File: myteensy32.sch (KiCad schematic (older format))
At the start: 14 parts, among them U1 MKL04Z32VLC4, U2 MK20DX256VLH7

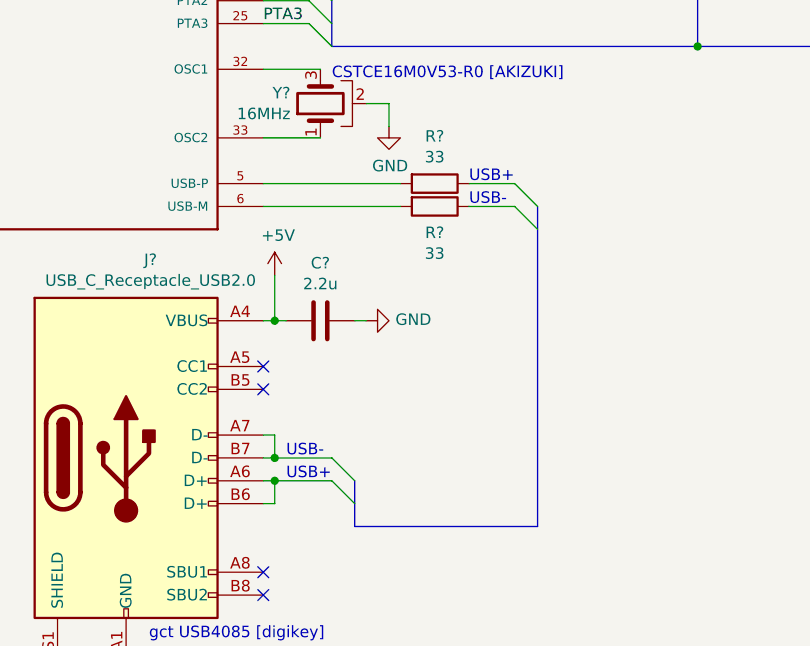
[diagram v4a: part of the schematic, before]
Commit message: ラベルのつもりがテキストになってたので修正
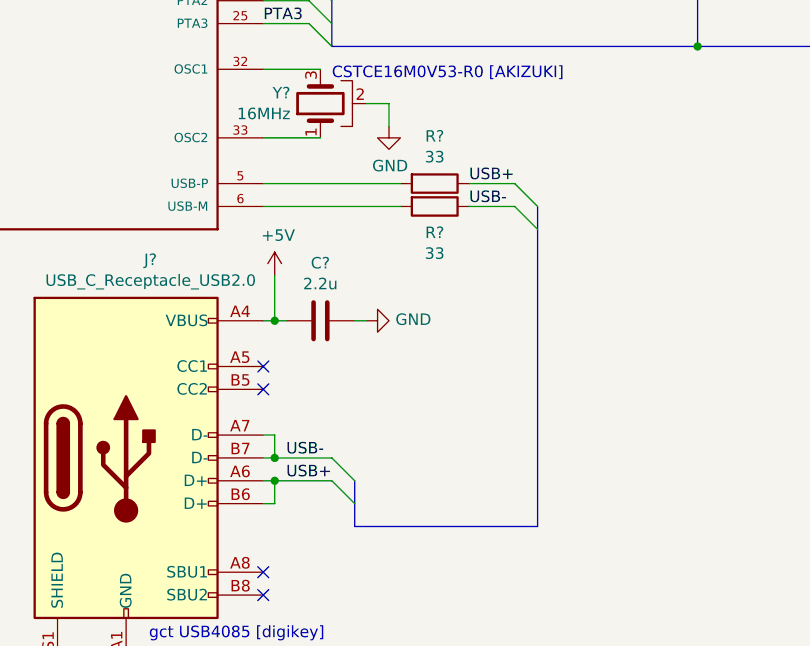
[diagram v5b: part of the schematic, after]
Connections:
- net USB+: now reaches J?.A6 (D+), J?.B6 (D+)
- net USB+: now also R?.1
- net USB-: now reaches J?.A7 (D-), J?.B7 (D-)
- net USB-: now also R?.1
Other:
- note removed: "USB+"
- note removed: "USB-"
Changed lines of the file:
@@
 Wire Wire Line
 	4850 5250 4650 5250
-Text Notes 4650 5250 0    50   ~ 0
-USB+
 Wire Wire Line
 	4650 5350 4850 5350
@@
 	1    0    0    -1
 $EndComp
-Text Notes 4650 5350 0    50   ~ 0
-USB-
 Wire Wire Line
 	3800 6450 3750 6450
@@
 	3800 6650 3750 6650
 Connection ~ 3800 6550
-Text Notes 3850 6550 0    50   ~ 0
-USB+
-Text Notes 3850 6450 0    50   ~ 0
-USB-
 $Comp
 L Device:R R?
@@
 Wire Bus Line
 	4050 4250 4050 4650
+Text Label 4650 5250 0    50   ~ 0
+USB+
+Text Label 4650 5350 0    50   ~ 0
+USB-
+Text Label 3850 6450 0    50   ~ 0
+USB-
+Text Label 3850 6550 0    50   ~ 0
+USB+
 $EndSCHEMATC

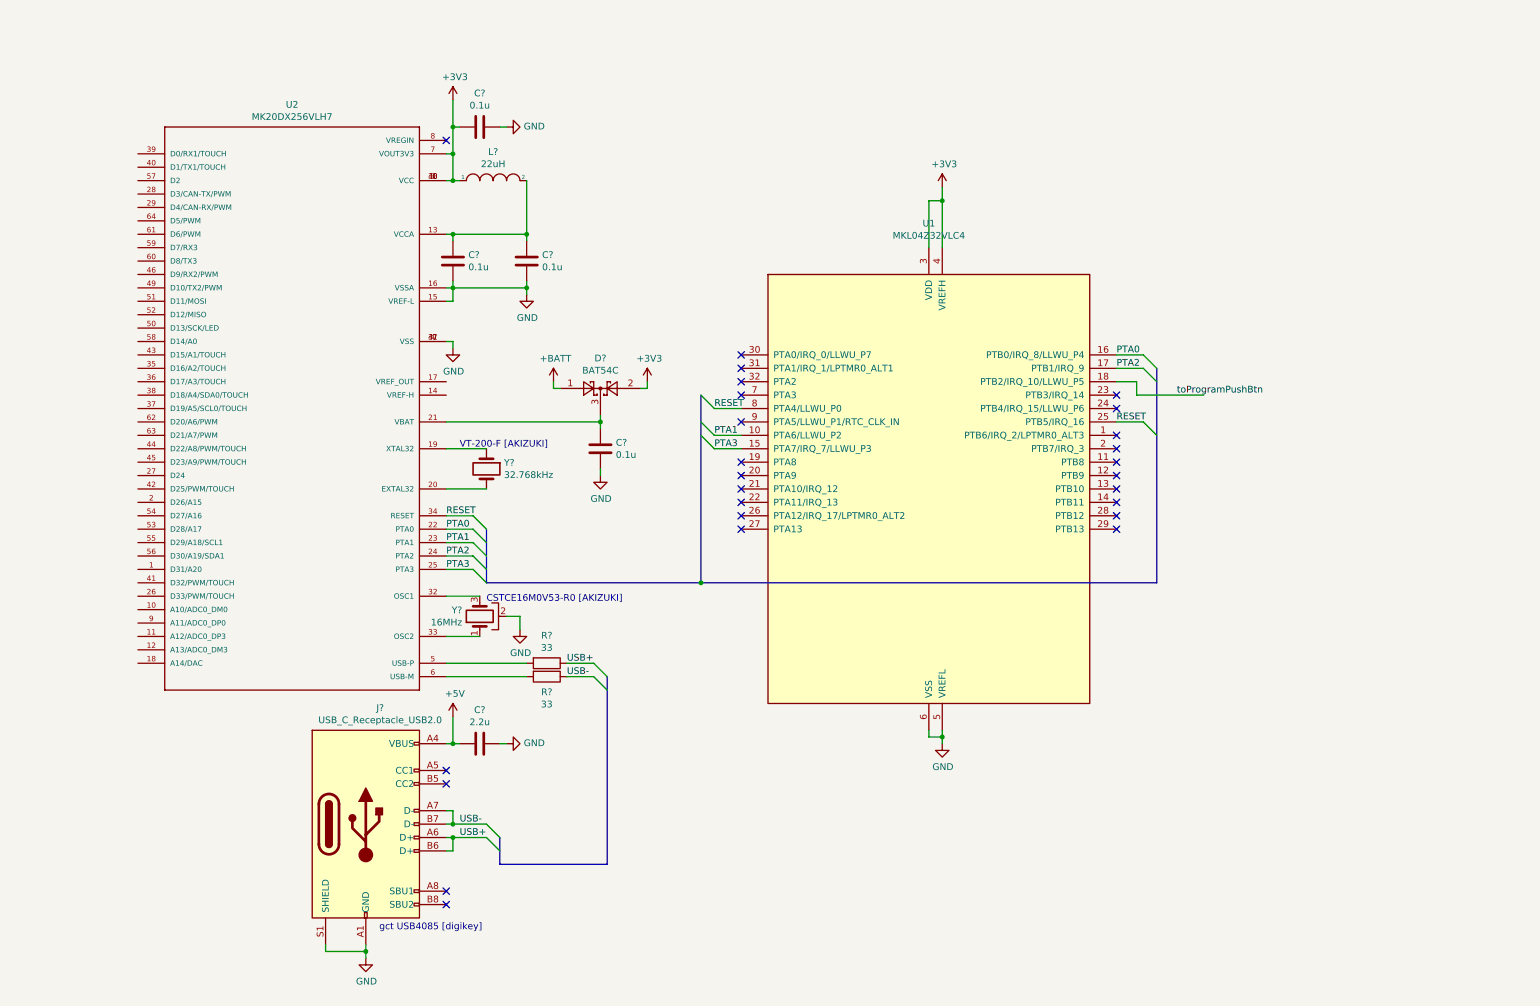
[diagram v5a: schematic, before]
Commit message: usb周辺回路、agnd等を記述
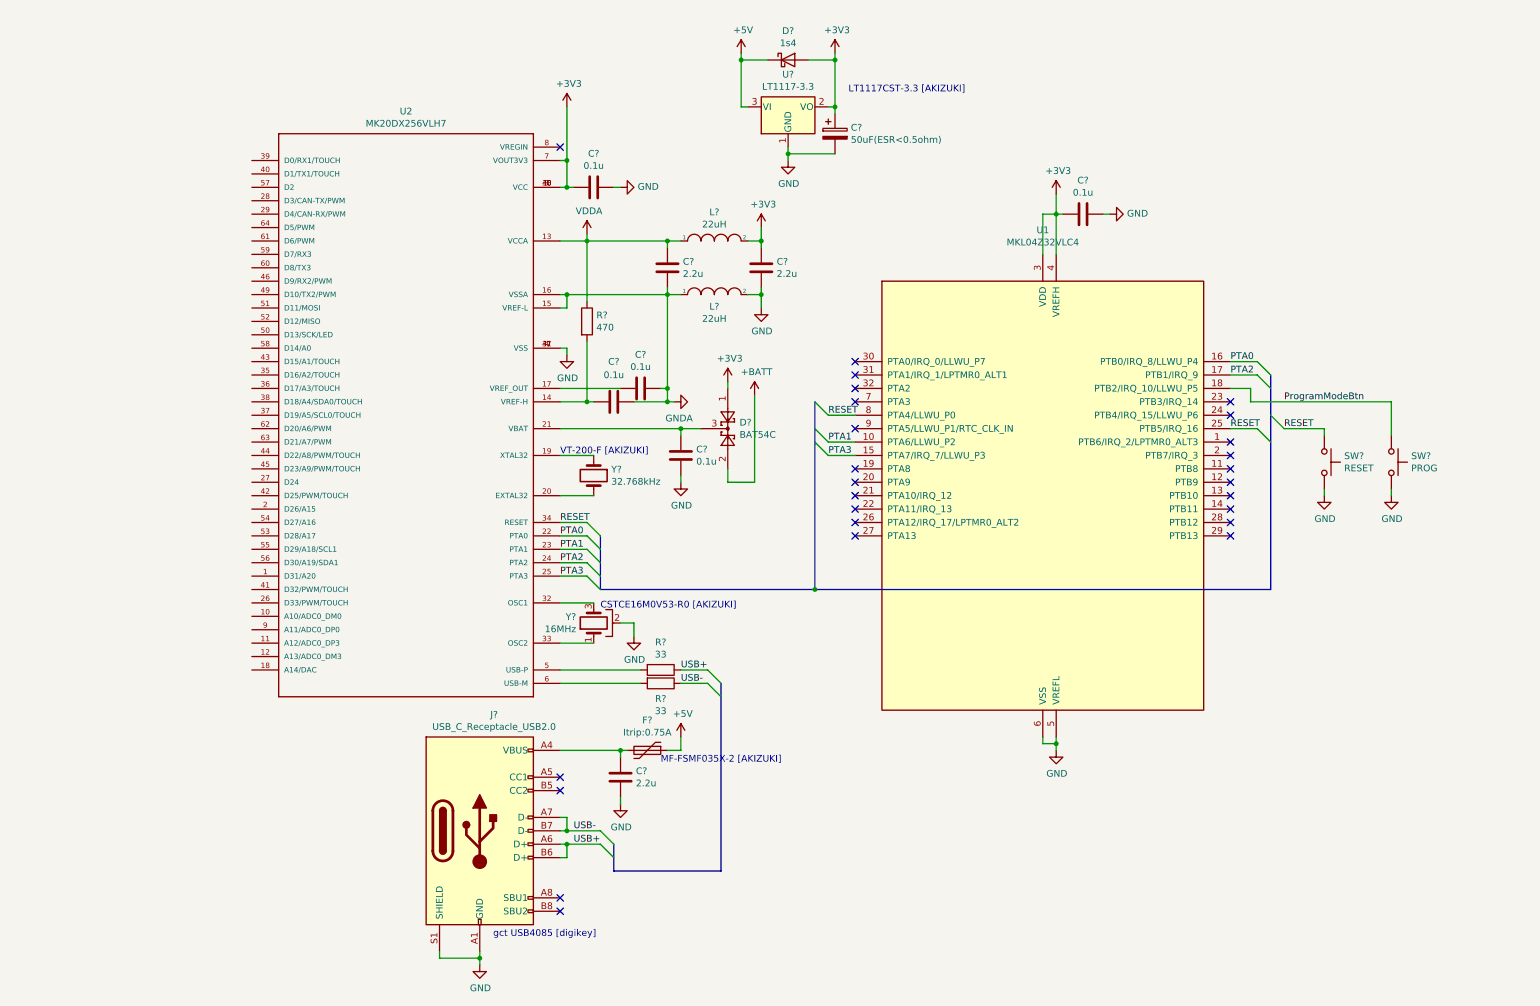
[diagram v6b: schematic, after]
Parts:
- added C? (x3): 0.1u, symbol Device:C
- added C?: 50uF(ESR<0.5ohm), symbol Device:CP
- added D?: 1s4, symbol Device:D_Schottky
- added F?: Itrip:0.75A, symbol Device:Polyfuse
- added L?: 22uH, symbol pspice:INDUCTOR
- added R?: 470, symbol Device:R
- added SW?: RESET, symbol Switch:SW_Push
- added SW?: PROG, symbol Switch:SW_Push
- added U?: LT1117-3.3, symbol Regulator_Linear:LT1117-3.3
- C? (x2): value 0.1u -> 2.2u
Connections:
- net +3V3: now also C?.1, D?.1, L?.2, C?.1, C?.2, D?.2 (A), U?.2 (VO); no longer D?.2, L?.1
- net +5V: now also D?.1 (K), F?.1, U?.3 (VI); no longer C?.2, J?.A4 (VBUS), J?.A9 (VBUS), J?.B4 (VBUS), J?.B9 (VBUS)
- net +BATT: now also D?.2; no longer D?.1
- net GND: now also C?.1, C?.2, L?.2, SW?.2, SW?.2, U?.1 (GND); no longer C?.2, U2.15 (VREF-L), U2.16 (VSSA)
- net RESET: now also SW?.1
- net VDDA: now reaches C?.1, U2.13 (VCCA)
- net VDDA: now also L?.1, R?.1; no longer C?.1, L?.2
- net at U2.14 (VREF-H): now also C?.2, R?.2
- net at U2.17 (VREF_OUT): now also C?.2
- net toProgramPushBtn renamed ProgramModeBtn
- net ProgramModeBtn: now also SW?.1
- new net: C?.2, F?.2, J?.A4 (VBUS), J?.A9 (VBUS), J?.B4 (VBUS), J?.B9 (VBUS)
- new net GNDA: C?.1, C?.1, C?.2, L?.1, U2.15 (VREF-L), U2.16 (VSSA)
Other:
- note added: "LT1117CST-3.3 [AKIZUKI]"
- note added: "MF-FSMF035X-2 [AKIZUKI]"
- moved on the sheet: C?, D?, J?, L?, R?, U1, U2, Y?

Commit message: とりあえず全部の素子にフットプリントを割り当てて大きさの余裕を見る。
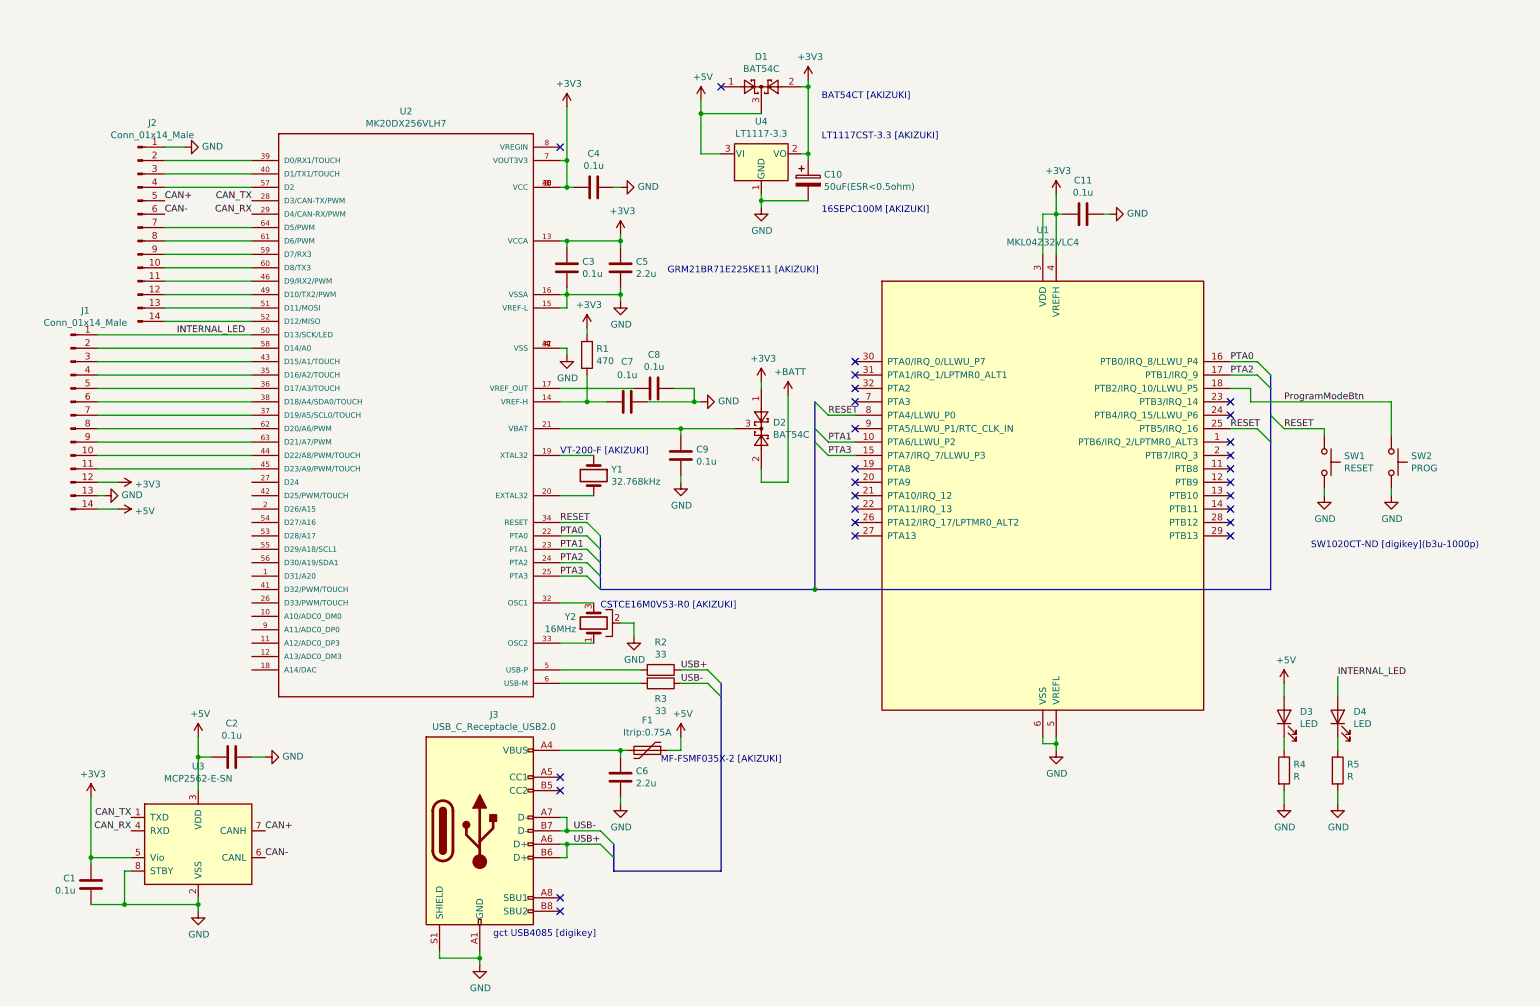
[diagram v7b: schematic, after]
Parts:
- removed C?: 2.2u, symbol Device:C
- removed D?: 1s4, symbol Device:D_Schottky
- removed L? (x2): 22uH, symbol pspice:INDUCTOR
- added C1, C2, C3: 0.1u, Capacitor_SMD:C_0603_1608Metric, symbol Device:C
- added D1: BAT54C, Package_TO_SOT_SMD:SOT-23, symbol Diode:BAT54C
- added D3, D4: LED, mylib:LED_1608_point, symbol Device:LED
- added J1, J2: Conn_01x14_Male, Connector_PinHeader_2.54mm:PinHeader_1x14_P2.54mm_Vertical, symbol Connector:Conn_01x14_Male
- added R4, R5: R, Resistor_SMD:R_0603_1608Metric, symbol Device:R
- added U3: MCP2562-E-SN, Package_SO:SOIC-8_3.9x4.9mm_P1.27mm, symbol Interface_CAN_LIN:MCP2562-E-SN
- C10: renamed from C?; footprint (none) -> Capacitor_THT:CP_Radial_D6.3mm_P2.50mm
- C11, C4, C7, C8, C9: renamed from C?; footprint (none) -> Capacitor_SMD:C_0603_1608Metric
- C5, C6: renamed from C?; footprint (none) -> Capacitor_SMD:C_0805_2012Metric
- F1: renamed from F?; footprint (none) -> Fuse:Fuse_0603_1608Metric
- J3: renamed from J?; footprint (none) -> Connector_USB:USB_C_Receptacle_GCT_USB4085
- R1, R2, R3: renamed from R?; footprint (none) -> Resistor_SMD:R_0603_1608Metric
- SW1, SW2: renamed from SW?; footprint (none) -> Button_Switch_SMD:SW_SPST_B3U-1000P
- U4: renamed from U?; footprint (none) -> Package_TO_SOT_SMD:SOT-223-3_TabPin2
- Y1: renamed from Y?; footprint (none) -> Crystal:Crystal_DS26_D2.0mm_L6.0mm_Horizontal
- Y2: renamed from Y?; footprint (none) -> mylib:CSTCE16M0V53-R0
- gave numbers to parts that had none: 1
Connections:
- net GNDA is gone; now on net GND: C5.2, C7.1, C8.1, U2.15 (VREF-L), U2.16 (VSSA)
- net VDDA is gone; now on net +3V3: C5.1, R1.1, U2.13 (VCCA)
- net +3V3: now also C1.2, C3.2, D1.2, J1.12 (Pin_12), U3.5 (Vio)
- net +5V: now also C2.2, D1.3, D3.2 (A), J1.14 (Pin_14), U3.3 (VDD)
- net GND: now also C1.1, C2.1, C3.1, J1.13 (Pin_13), J2.1 (Pin_1), R4.2, R5.2, U3.2 (VSS), U3.8 (STBY)
- net CAN_TX: now reaches U2.28 (D3/CAN-TX/PWM)
- net CAN_TX: now also U3.1 (TXD)
- net CAN_RX: now reaches U2.29 (D4/CAN-RX/PWM)
- net CAN_RX: now also U3.4 (RXD)
- net at U2.35 (D16/A2/TOUCH): now also J1.4 (Pin_4)
- net at U2.36 (D17/A3/TOUCH): now also J1.5 (Pin_5)
- net at U2.37 (D19/A5/SCL0/TOUCH): now also J1.7 (Pin_7)
- net at U2.38 (D18/A4/SDA0/TOUCH): now also J1.6 (Pin_6)
- net at U2.39 (D0/RX1/TOUCH): now also J2.2 (Pin_2)
- net at U2.40 (D1/TX1/TOUCH): now also J2.3 (Pin_3)
- net at U2.43 (D15/A1/TOUCH): now also J1.3 (Pin_3)
- net at U2.44 (D22/A8/PWM/TOUCH): now also J1.10 (Pin_10)
- net at U2.45 (D23/A9/PWM/TOUCH): now also J1.11 (Pin_11)
- net at U2.46 (D9/RX2/PWM): now also J2.11 (Pin_11)
- net at U2.49 (D10/TX2/PWM): now also J2.12 (Pin_12)
- net INTERNAL_LED: now reaches U2.50 (D13/SCK/LED)
- net INTERNAL_LED: now also D4.2 (A), J1.1 (Pin_1)
- net at U2.51 (D11/MOSI): now also J2.13 (Pin_13)
- net at U2.52 (D12/MISO): now also J2.14 (Pin_14)
- net at U2.57 (D2): now also J2.4 (Pin_4)
- net at U2.58 (D14/A0): now also J1.2 (Pin_2)
- net at U2.59 (D7/RX3): now also J2.9 (Pin_9)
- net at U2.60 (D8/TX3): now also J2.10 (Pin_10)
- net at U2.61 (D6/PWM): now also J2.8 (Pin_8)
- net at U2.62 (D20/A6/PWM): now also J1.8 (Pin_8)
- net at U2.63 (D21/A7/PWM): now also J1.9 (Pin_9)
- net at U2.64 (D5/PWM): now also J2.7 (Pin_7)
- new net: D3.1 (K), R4.1
- new net: D4.1 (K), R5.1
- new net CAN+: J2.5 (Pin_5), U3.7 (CANH)
- new net CAN-: J2.6 (Pin_6), U3.6 (CANL)
- no-connect marks 26 -> 27
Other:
- note added: "16SEPC100M [AKIZUKI]"
- note added: "BAT54CT [AKIZUKI]"
- note added: "GRM21BR71E225KE11 [AKIZUKI]"
- note added: "SW1020CT-ND [digikey](b3u-1000p)"
- moved on the sheet: C10, C5, C7, C8, D2, R1, U4

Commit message: rtc用の水晶は面積の問題と使わないので削除
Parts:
- removed Y1: 32.768kHz, Crystal:Crystal_DS26_D2.0mm_L6.0mm_Horizontal, symbol Device:Crystal
- C10: footprint Capacitor_THT:CP_Radial_D6.3mm_P2.50mm -> Capacitor_SMD:C_1206_3216Metric
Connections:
- net +BATT: no longer names the net of D2.2
- no-connect marks 27 -> 30
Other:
- note added: "JMK316ABJ107ML-T [AKIZUKI](100uF,6.3v)"
- note removed: "16SEPC100M [AKIZUKI]"
- note removed: "VT-200-F [AKIZUKI]"
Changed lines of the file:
@@
 	1    0    0    -1
 $EndComp
-$Comp
-L Device:Crystal Y1
-U 1 1 5F4C8EEC
-P 4850 3850
-F 0 "Y1" V 4804 3981 50  0000 L CNN
-F 1 "32.768kHz" V 4895 3981 50  0000 L CNN
-F 2 "Crystal:Crystal_DS26_D2.0mm_L6.0mm_Horizontal" H 4850 3850 50  0001 C CNN
-F 3 "~" H 4850 3850 50  0001 C CNN
-	1    4850 3850
-	0    1    1    0
-$EndComp
-Wire Wire Line
-	4850 3700 4600 3700
-Wire Wire Line
-	4850 4000 4600 4000
 Wire Wire Line
 	4850 4800 4600 4800
@@
 Wire Wire Line
 	5150 4950 5050 4950
-Text Notes 4600 3700 0    50   ~ 0
-VT-200-F [AKIZUKI]
 $Comp
 L Diode:BAT54C D2
@@
 Wire Wire Line
 	6100 3150 6100 3200
-$Comp
-L power:+BATT #PWR0106
-U 1 1 5F5089FA
-P 6300 3250
-F 0 "#PWR0106" H 6300 3100 50  0001 C CNN
-F 1 "+BATT" H 6315 3423 50  0000 C CNN
-F 2 "" H 6300 3250 50  0001 C CNN
-F 3 "" H 6300 3250 50  0001 C CNN
-	1    6300 3250
-	1    0    0    -1
-$EndComp
-Wire Wire Line
-	6300 3250 6300 3900
 $Comp
 L power:+3V3 #PWR0107
@@
 Connection ~ 5500 3500
 Wire Wire Line
-	6300 3900 6100 3900
-Wire Wire Line
-	6100 3900 6100 3800
-Wire Wire Line
 	4650 2950 4650 2900
 Wire Wire Line
@@
 F 0 "C10" H 6568 1696 50  0000 L CNN
 F 1 "50uF(ESR<0.5ohm)" H 6568 1605 50  0000 L CNN
-F 2 "Capacitor_THT:CP_Radial_D6.3mm_P2.50mm" H 6488 1500 50  0001 C CNN
+F 2 "Capacitor_SMD:C_1206_3216Metric" H 6488 1500 50  0001 C CNN
 F 3 "~" H 6450 1650 50  0001 C CNN
 	1    6450 1650
@@
 	5650 1150 5650 1450
 NoConn ~ 5800 950
-Wire Bus Line
-	9900 3400 9900 3600
-Wire Bus Line
-	9900 3600 9900 4700
-Wire Bus Line
-	6500 3600 6500 4700
-Wire Bus Line
-	4900 4500 4900 4600
-Wire Bus Line
-	4900 4600 4900 4700
-Wire Bus Line
-	4900 4400 4900 4500
-Wire Bus Line
-	4900 4300 4900 4400
-Wire Bus Line
-	9900 3200 9900 3400
-Wire Bus Line
-	9900 3100 9900 3200
-Wire Bus Line
-	6500 3500 6500 3600
-Wire Bus Line
-	6500 3300 6500 3500
-Wire Bus Line
-	5800 5500 5800 6800
-Wire Bus Line
-	5800 5400 5800 5500
-Wire Bus Line
-	5000 6700 5000 6800
-Wire Bus Line
-	5000 6600 5000 6700
 Text Notes 10200 4400 0    50   ~ 0
 SW1020CT-ND [digikey](b3u-1000p)
@@
 GRM21BR71E225KE11 [AKIZUKI]
 Text Notes 6550 1900 0    50   ~ 0
-16SEPC100M [AKIZUKI]
+JMK316ABJ107ML-T [AKIZUKI](100uF,6.3v)
+NoConn ~ 4600 3700
+NoConn ~ 4600 4000
+NoConn ~ 6100 3800
+Wire Bus Line
+	5800 5400 5800 6800
+Wire Bus Line
+	5000 6600 5000 6800
+Wire Bus Line
+	6500 3300 6500 4700
+Wire Bus Line
+	9900 3100 9900 4700
+Wire Bus Line
+	4900 4300 4900 4700
 $EndSCHEMATC
